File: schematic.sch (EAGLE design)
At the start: 36 parts, among them X1 SSW-108-02-S-D-RA, X2 SSW-116-02-S-TRA, X3 SSW-106-02-S-D-RA, X4 SSW-116-02-S-TRA

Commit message: Connectorizing and adding switches.
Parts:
- removed PAD5, PAD6, PAD7, PAD8: WIREPAD4,16O1,6, wirepad:WIREPAD4,16O1,6
- added C5, C6, C7, C8: (no value), rcl:C-USC0805
- added JP1, JP2: (no value), pinhead:PINHD-1X3
- added LED1, LED2: (no value), led:LEDCHIPLED_0805
- added PAD10, PAD9: WIREPAD4,16O1,6, wirepad:WIREPAD4,16O1,6
- added R10, R11, R12, R13, R14, R15, R5, R6, R7, R8, R9: (no value), rcl:R-US_M0805
- added U$17, U$25, U$26: INA139, ti:INA139
- added U$18: DF13-6, df13:DF13-6
- added U$19, U$36: 30R110U, littelfuse:30R110U
- added U$20, U$30, U$31, U$32, U$33, U$35, U$47: 30R250U, littelfuse:30R250U
- added U$21, U$22, U$23, U$24, U$34, U$46: MED_MOSFET, pololu:MED_MOSFET
- added U$27: DF13-5, df13:DF13-5
- added U$28, U$29: M2022LL2W13, switch:M2022LL2W13
- added U$37, U$38, U$39: JST-PA-4, jst:JST-PA-4
- added U$40, U$41, U$48, U$49: JST-PA-3, jst:JST-PA-3
- added U$42, U$43, U$44, U$45: JST-PA-2, jst:JST-PA-2
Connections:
- removed net N$2: C1.1, PAD4.P, U$1.ON/OFF, U$1.VIN+
- new net 24V_CUR_MEAS: C8.1, R12.1, U$26.OUT, U$27.P4
- new net 24V_ONOFF: U$2.ON/OFF, U$29.1A, U$29.1A1
- new net 5V_CUR_MEAS: C7.1, R10.1, U$25.OUT, U$27.P2
- new net 5V_ONOFF: U$1.ON/OFF, U$28.1A, U$28.1A1
- new net CUR_MEAS: C6.1, R6.1, U$17.OUT, U$18.P3
- new net N$10: PAD9.P, U$20.1
- new net N$12: PAD1.P, R5.1, R7.2, U$17.V+, U$17.VIN-
- new net N$13: R3.1, R9.1, U$1.SENSE+, U$1.VOUT+, U$25.V+, U$25.VIN-
- new net N$15: U$18.P1, U$18.P2, U$19.1
- new net N$16: JP2.2, U$23.LOAD_HIGH1, U$23.LOAD_HIGH2, U$23.LOAD_HIGH3, U$23.LOAD_HIGH4
- new net N$17: R1.1, R11.1, U$2.SENSE+, U$2.VOUT+, U$26.V+, U$26.VIN-
- new net N$18: LED2.C, R14.2
- new net N$19: LED1.C, R13.2
- new net V_MEAS: C5.1, R7.1, R8.2, U$18.P4
- net +24V: now also JP1.1, JP2.1, LED2.A, R11.2, U$20.2, U$21.LOAD_HIGH1, U$21.LOAD_HIGH2, U$21.LOAD_HIGH3, U$21.LOAD_HIGH4, U$24.LOAD_HIGH1, U$24.LOAD_HIGH2, U$24.LOAD_HIGH3, U$24.LOAD_HIGH4, U$26.VIN+, U$34.LOAD_HIGH1, U$34.LOAD_HIGH2, U$34.LOAD_HIGH3, U$34.LOAD_HIGH4, U$46.LOAD_HIGH1, U$46.LOAD_HIGH2, U$46.LOAD_HIGH3, U$46.LOAD_HIGH4; no longer R1.1, U$13.2, U$2.SENSE+, U$2.VOUT+
- net +5V: now also JP1.3, JP2.3, LED1.A, R9.2, U$19.2, U$21.5V, U$22.5V, U$23.5V, U$24.5V, U$25.VIN+, U$30.2, U$34.5V, U$46.5V; no longer R3.1, U$1.SENSE+, U$1.VOUT+
- net AUX1: now also U$21.PWM, U$24.PWM
- net AUX2: now also U$34.PWM, U$46.PWM
- net AUX3: now also U$22.PWM
- net AUX4: now also U$23.PWM
- net AUX5: now also R15.2
- net GND: now also C5.2, C6.2, C7.2, C8.2, PAD10.P, PAD4.P, R10.2, R12.2, R13.1, R14.1, R15.1, R6.2, R8.1, U$14.GND1, U$14.GND2, U$14.P6, U$17.GND, U$18.GND1, U$18.GND2, U$18.P5, U$18.P6, U$21.GND, U$21.GND1, U$21.GND2, U$21.GND3, U$22.GND, U$22.GND1, U$22.GND2, U$22.GND3, U$23.GND, U$23.GND1, U$23.GND2, U$23.GND3, U$24.GND, U$24.GND1, U$24.GND2, U$24.GND3, U$25.GND, U$26.GND, U$27.GND1, U$27.GND2, U$27.P3, U$27.P5, U$28.GND1, U$28.GND2, U$28.GND3, U$28.GND4, U$28.NO, U$28.NO1, U$29.GND1, U$29.GND2, U$29.GND3, U$29.GND4, U$29.NO, U$29.NO1, U$34.GND, U$34.GND1, U$34.GND2, U$34.GND3, U$46.GND, U$46.GND1, U$46.GND2, U$46.GND3; no longer PAD6.P, U$14.P$6, U$14.P$7, U$14.P$8
- net N$1: now also PAD3.P, U$30.1; no longer C2.1, PAD8.P, U$2.ON/OFF, U$2.VIN+
- net N$4: now also JP1.2, U$22.LOAD_HIGH1, U$22.LOAD_HIGH2, U$22.LOAD_HIGH3, U$22.LOAD_HIGH4; no longer PAD5.P, U$13.1
- net RCTS: now also U$14.P4; no longer U$14.P$4
- net RRTS: now also U$14.P5; no longer U$14.P$5
- net RRX: now also U$14.P2; no longer U$14.P$2
- net RTX: now also U$14.P3; no longer U$14.P$3
- net V+: now also C1.1, C2.1, R5.2, U$1.VIN+, U$17.VIN+, U$2.VIN+, U$28.NC, U$28.NC1, U$29.NC, U$29.NC1; no longer PAD1.P, PAD3.P, PAD7.P
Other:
- note added: "Fused Servo Output"
- note added: "Landing Lights"
- note added: "Lidar Lite Connection"
- note added: "Payload Switched Output 1"
- note added: "Payload Switched Output 2"
- note added: "Pixhawk Connection"
- note added: "RFD900 Interface"
- note added: "Raspberry Pi"
- note added: "Taxi Lights"
- note added: "WiFi PoE Adapter"
- note added: "Wing Strobe / Anti Collision"
- note added: "Wing Tip"
- note added: "X4r Interface"
- note removed: "Pin"
- note removed: "Socket"

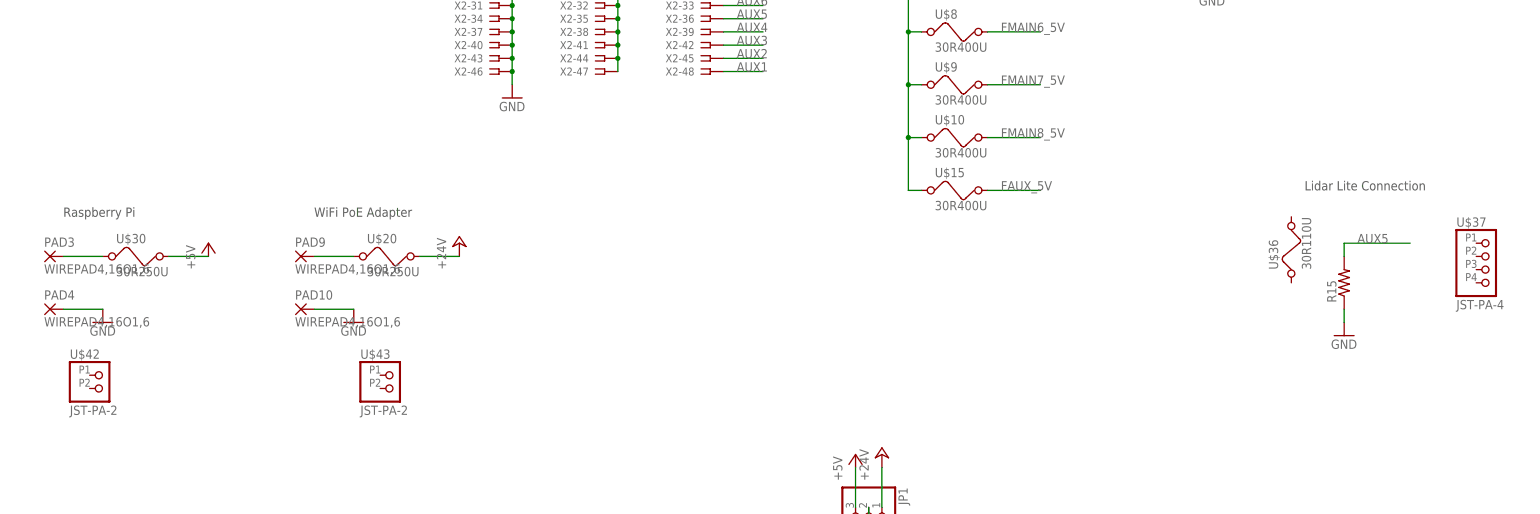
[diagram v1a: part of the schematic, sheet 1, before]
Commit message: Connecting power connectors and lidar lite.
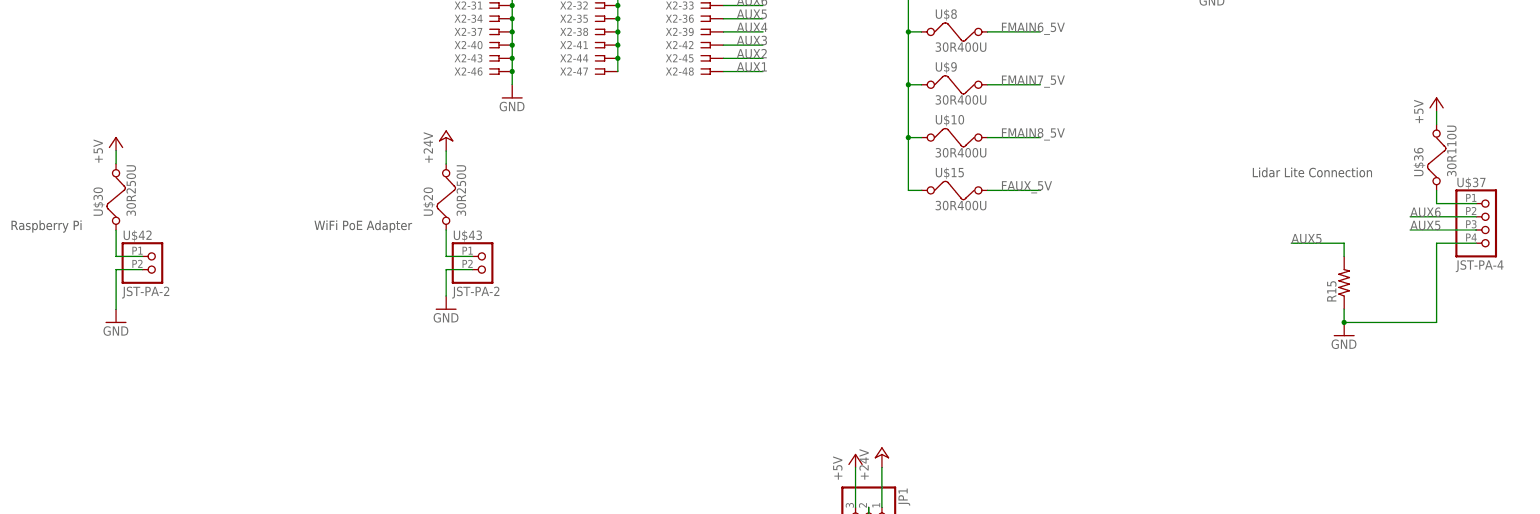
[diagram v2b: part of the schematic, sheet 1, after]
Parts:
- removed PAD10, PAD3, PAD4, PAD9: WIREPAD4,16O1,6, wirepad:WIREPAD4,16O1,6
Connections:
- new net N$2: U$36.1, U$37.1
- net +5V: now also U$36.2
- net AUX5: now also U$37.3
- net AUX6: now also U$37.2
- net GND: now also U$37.4, U$42.2, U$43.2; no longer PAD10.P, PAD4.P
- net N$1: now also U$42.1; no longer PAD3.P
- net N$10: now also U$43.1; no longer PAD9.P
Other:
- moved on the sheet: U$20, U$30, U$36, U$37, U$42, U$43
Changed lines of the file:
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@@
 <part name="P+11" library="supply1" deviceset="+5V" device=""/>
 <part name="U$20" library="littelfuse" deviceset="30R250U" device=""/>
-<part name="PAD9" library="wirepad" deviceset="WIREPAD" device="4,16O1,6"/>
-<part name="PAD10" library="wirepad" deviceset="WIREPAD" device="4,16O1,6"/>
 <part name="P+12" library="supply1" deviceset="+24V" device=""/>
 <part name="GND13" library="supply1" deviceset="GND" device=""/>
@@
 <part name="GND28" library="supply1" deviceset="GND" device=""/>
 <part name="U$30" library="littelfuse" deviceset="30R250U" device=""/>
-<part name="PAD3" library="wirepad" deviceset="WIREPAD" device="4,16O1,6"/>
-<part name="PAD4" library="wirepad" deviceset="WIREPAD" device="4,16O1,6"/>
 <part name="GND29" library="supply1" deviceset="GND" device=""/>
 <part name="P+17" library="supply1" deviceset="+5V" device=""/>
@@
 <part name="U$48" library="jst" deviceset="JST-PA-3" device=""/>
 <part name="U$49" library="jst" deviceset="JST-PA-3" device=""/>
+<part name="P+31" library="supply1" deviceset="+5V" device=""/>
 </parts>
 <sheets>
 <sheet>
 <plain>
-<text x="48.26" y="-27.94" size="1.778" layer="97">WiFi PoE Adapter</text>
+<text x="48.26" y="-30.48" size="1.778" layer="97">WiFi PoE Adapter</text>
 <text x="121.92" y="-91.44" size="1.778" layer="97">Payload Switched Output 1</text>
 <text x="43.18" y="-91.44" size="1.778" layer="97">Wing Tip</text>
 <text x="40.64" y="-139.7" size="1.778" layer="97">Wing Strobe / Anti Collision</text>
 <text x="124.46" y="-139.7" size="1.778" layer="97">Payload Switched Output 2</text>
-<text x="0" y="-27.94" size="1.778" layer="97">Raspberry Pi</text>
+<text x="-10.16" y="-30.48" size="1.778" layer="97">Raspberry Pi</text>
 <text x="78.74" y="45.72" size="1.778" layer="97">Pixhawk Connection</text>
 <text x="215.9" y="66.04" size="1.778" layer="97">Fused Servo Output</text>
 <text x="43.18" y="-185.42" size="1.778" layer="97">Taxi Lights</text>
-<text x="238.76" y="-22.86" size="1.778" layer="97">Lidar Lite Connection</text>
+<text x="228.6" y="-20.32" size="1.778" layer="97">Lidar Lite Connection</text>
 <text x="43.18" y="-223.52" size="1.778" layer="97">Landing Lights</text>
 </plain>
@@
 <instance part="U$16" gate="G$1" x="106.68" y="50.8" rot="R90"/>
 <instance part="P+9" gate="1" x="106.68" y="60.96"/>
-<instance part="U$20" gate="G$1" x="63.5" y="-35.56"/>
-<instance part="PAD9" gate="G$1" x="45.72" y="-35.56"/>
-<instance part="PAD10" gate="G$1" x="45.72" y="-45.72"/>
-<instance part="P+12" gate="1" x="76.2" y="-33.02"/>
-<instance part="GND13" gate="1" x="55.88" y="-48.26"/>
+<instance part="U$20" gate="G$1" x="73.66" y="-22.86" rot="R90"/>
+<instance part="P+12" gate="1" x="73.66" y="-12.7"/>
+<instance part="GND13" gate="1" x="73.66" y="-45.72"/>
 <instance part="U$21" gate="G$1" x="55.88" y="-104.14"/>
 <instance part="U$22" gate="G$1" x="134.62" y="-104.14"/>
@@
 <instance part="JP2" gate="A" x="157.48" y="-134.62" rot="R270"/>
 <instance part="P+22" gate="1" x="154.94" y="-121.92"/>
-<instance part="U$30" gate="G$1" x="15.24" y="-35.56"/>
-<instance part="PAD3" gate="G$1" x="-2.54" y="-35.56"/>
-<instance part="PAD4" gate="G$1" x="-2.54" y="-45.72"/>
-<instance part="GND29" gate="1" x="7.62" y="-48.26"/>
-<instance part="P+17" gate="1" x="27.94" y="-33.02"/>
+<instance part="U$30" gate="G$1" x="10.16" y="-22.86" rot="R90"/>
+<instance part="GND29" gate="1" x="10.16" y="-48.26"/>
+<instance part="P+17" gate="1" x="10.16" y="-12.7"/>
 <instance part="U$13" gate="G$1" x="86.36" y="-104.14"/>
 <instance part="U$31" gate="G$1" x="86.36" y="-152.4"/>
@@
 <instance part="R15" gate="G$1" x="246.38" y="-40.64" rot="R90"/>
 <instance part="GND30" gate="1" x="246.38" y="-50.8"/>
-<instance part="U$36" gate="G$1" x="236.22" y="-33.02" rot="R90"/>
-<instance part="U$37" gate="G$1" x="271.78" y="-35.56"/>
+<instance part="U$36" gate="G$1" x="264.16" y="-15.24" rot="R90"/>
+<instance part="U$37" gate="G$1" x="271.78" y="-27.94"/>
 <instance part="U$38" gate="G$1" x="99.06" y="-119.38"/>
 <instance part="U$39" gate="G$1" x="99.06" y="-142.24"/>
 <instance part="U$40" gate="G$1" x="99.06" y="-165.1"/>
 <instance part="U$41" gate="G$1" x="99.06" y="-99.06"/>
-<instance part="U$42" gate="G$1" x="5.08" y="-58.42"/>
-<instance part="U$43" gate="G$1" x="60.96" y="-58.42"/>
+<instance part="U$42" gate="G$1" x="15.24" y="-35.56"/>
+<instance part="U$43" gate="G$1" x="78.74" y="-35.56"/>
 <instance part="U$44" gate="G$1" x="180.34" y="-101.6"/>
 <instance part="U$45" gate="G$1" x="180.34" y="-154.94"/>
@@
 <instance part="U$48" gate="G$1" x="101.6" y="-198.12"/>
 <instance part="U$49" gate="G$1" x="101.6" y="-220.98"/>
+<instance part="P+31" gate="1" x="264.16" y="-5.08"/>
 </instances>
 <busses>
@@
 <pinref part="U$20" gate="G$1" pin="2"/>
 <pinref part="P+12" gate="1" pin="+24V"/>
-<wire x1="76.2" y1="-35.56" x2="68.58" y2="-35.56" width="0.1524" layer="91"/>
+<wire x1="73.66" y1="-15.24" x2="73.66" y2="-17.78" width="0.1524" layer="91"/>
 </segment>
 <segment>
@@
 </segment>
 <segment>
-<pinref part="PAD10" gate="G$1" pin="P"/>
-<pinref part="GND13" gate="1" pin="GND"/>
-<wire x1="48.26" y1="-45.72" x2="55.88" y2="-45.72" width="0.1524" layer="91"/>
-</segment>
-<segment>
 <pinref part="GND14" gate="1" pin="GND"/>
 <pinref part="U$21" gate="G$1" pin="GND3"/>
@@
 </segment>
 <segment>
-<pinref part="PAD4" gate="G$1" pin="P"/>
 <pinref part="GND29" gate="1" pin="GND"/>
-<wire x1="0" y1="-45.72" x2="7.62" y2="-45.72" width="0.1524" layer="91"/>
+<pinref part="U$42" gate="G$1" pin="2"/>
+<wire x1="10.16" y1="-45.72" x2="10.16" y2="-38.1" width="0.1524" layer="91"/>
+<wire x1="10.16" y1="-38.1" x2="15.24" y2="-38.1" width="0.1524" layer="91"/>
 </segment>
 <segment>
@@
 <pinref part="R15" gate="G$1" pin="1"/>
 <wire x1="246.38" y1="-48.26" x2="246.38" y2="-45.72" width="0.1524" layer="91"/>
+<wire x1="246.38" y1="-48.26" x2="264.16" y2="-48.26" width="0.1524" layer="91"/>
+<wire x1="264.16" y1="-48.26" x2="264.16" y2="-33.02" width="0.1524" layer="91"/>
+<junction x="246.38" y="-48.26"/>
+<pinref part="U$37" gate="G$1" pin="4"/>
+<wire x1="264.16" y1="-33.02" x2="271.78" y2="-33.02" width="0.1524" layer="91"/>
 </segment>
 <segment>
@@
 <wire x1="35.56" y1="-236.22" x2="35.56" y2="-238.76" width="0.1524" layer="91"/>
 <junction x="35.56" y="-238.76"/>
+</segment>
+<segment>
+<pinref part="GND13" gate="1" pin="GND"/>
+<pinref part="U$43" gate="G$1" pin="2"/>
+<wire x1="73.66" y1="-43.18" x2="73.66" y2="-38.1" width="0.1524" layer="91"/>
+<wire x1="73.66" y1="-38.1" x2="78.74" y2="-38.1" width="0.1524" layer="91"/>
 </segment>
 </net>
@@
 <segment>
 <pinref part="U$30" gate="G$1" pin="2"/>
-<wire x1="27.94" y1="-35.56" x2="20.32" y2="-35.56" width="0.1524" layer="91"/>
+<wire x1="10.16" y1="-15.24" x2="10.16" y2="-17.78" width="0.1524" layer="91"/>
 <pinref part="P+17" gate="1" pin="+5V"/>
 </segment>
@@
 <wire x1="35.56" y1="-228.6" x2="35.56" y2="-226.06" width="0.1524" layer="91"/>
 </segment>
+<segment>
+<pinref part="U$36" gate="G$1" pin="2"/>
+<pinref part="P+31" gate="1" pin="+5V"/>
+<wire x1="264.16" y1="-10.16" x2="264.16" y2="-7.62" width="0.1524" layer="91"/>
+</segment>
 </net>
 <net name="RC_SIG" class="0">
@@
 <pinref part="R15" gate="G$1" pin="2"/>
 <wire x1="246.38" y1="-35.56" x2="246.38" y2="-33.02" width="0.1524" layer="91"/>
-<wire x1="246.38" y1="-33.02" x2="259.08" y2="-33.02" width="0.1524" layer="91"/>
-<label x="248.92" y="-33.02" size="1.778" layer="95"/>
+<wire x1="246.38" y1="-33.02" x2="236.22" y2="-33.02" width="0.1524" layer="91"/>
+<label x="236.22" y="-33.02" size="1.778" layer="95"/>
+</segment>
+<segment>
+<pinref part="U$37" gate="G$1" pin="3"/>
+<wire x1="271.78" y1="-30.48" x2="259.08" y2="-30.48" width="0.1524" layer="91"/>
+<label x="259.08" y="-30.48" size="1.778" layer="95"/>
 </segment>
 </net>
@@
 <wire x1="261.62" y1="48.26" x2="271.78" y2="48.26" width="0.1524" layer="91"/>
 <label x="264.16" y="48.26" size="1.778" layer="95"/>
+</segment>
+<segment>
+<pinref part="U$37" gate="G$1" pin="2"/>
+<wire x1="271.78" y1="-27.94" x2="259.08" y2="-27.94" width="0.1524" layer="91"/>
+<label x="259.08" y="-27.94" size="1.778" layer="95"/>
 </segment>
 </net>
@@
 <net name="N$10" class="0">
 <segment>
-<pinref part="PAD9" gate="G$1" pin="P"/>
 <pinref part="U$20" gate="G$1" pin="1"/>
-<wire x1="55.88" y1="-35.56" x2="48.26" y2="-35.56" width="0.1524" layer="91"/>
+<pinref part="U$43" gate="G$1" pin="1"/>
+<wire x1="73.66" y1="-30.48" x2="73.66" y2="-35.56" width="0.1524" layer="91"/>
+<wire x1="73.66" y1="-35.56" x2="78.74" y2="-35.56" width="0.1524" layer="91"/>
 </segment>
 </net>
@@
 <net name="N$1" class="0">
 <segment>
-<pinref part="PAD3" gate="G$1" pin="P"/>
 <pinref part="U$30" gate="G$1" pin="1"/>
-<wire x1="7.62" y1="-35.56" x2="0" y2="-35.56" width="0.1524" layer="91"/>
+<pinref part="U$42" gate="G$1" pin="1"/>
+<wire x1="15.24" y1="-35.56" x2="10.16" y2="-35.56" width="0.1524" layer="91"/>
+<wire x1="10.16" y1="-35.56" x2="10.16" y2="-30.48" width="0.1524" layer="91"/>
 </segment>
 </net>
@@
 </segment>
 </net>
+<net name="N$2" class="0">
+<segment>
+<pinref part="U$37" gate="G$1" pin="1"/>
+<pinref part="U$36" gate="G$1" pin="1"/>
+<wire x1="271.78" y1="-25.4" x2="264.16" y2="-25.4" width="0.1524" layer="91"/>
+<wire x1="264.16" y1="-25.4" x2="264.16" y2="-22.86" width="0.1524" layer="91"/>
+</segment>
+</net>
